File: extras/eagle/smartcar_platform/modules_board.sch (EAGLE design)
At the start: 40 parts

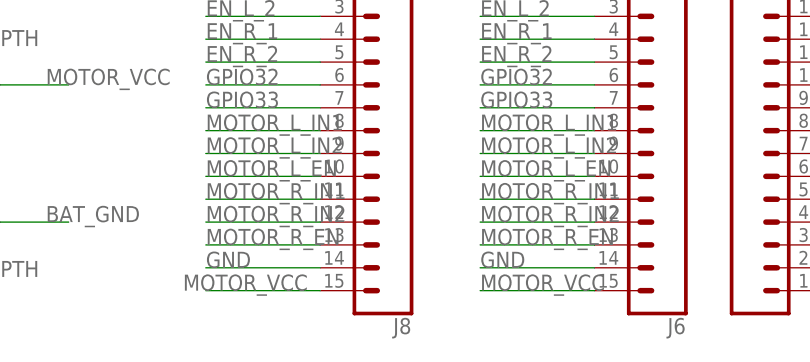
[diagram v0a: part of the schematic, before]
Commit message: Fix ESP32 power supply line to 5V
ESP32 was powered on via its VIN pin which based
on the specs of the ESP32 DOIT devkit is supposed
to handle up to 12V.
This isn't actually the case and anything above 6V
makes the regulator on the board overheat.

Note that the 5V is actually the voltage coming from
our own on-board regulator.
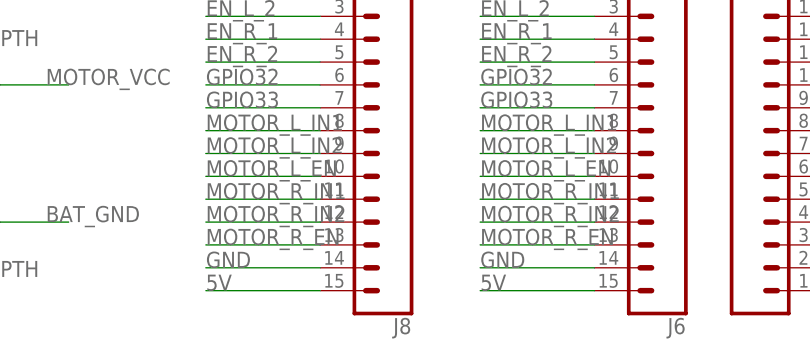
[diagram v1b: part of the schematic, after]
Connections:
- net 5V: now also J6.15, J8.15
- net MOTOR_VCC: no longer J6.15, J8.15
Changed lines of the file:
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@@
 <?xml version="1.0" encoding="utf-8"?>
 <!DOCTYPE eagle SYSTEM "eagle.dtd">
-<eagle version="9.5.2">
+<eagle version="9.6.2">
 <drawing>
 <settings>
@@
 </segment>
 <segment>
-<pinref part="J6" gate="G$1" pin="15"/>
-<wire x1="-73.66" y1="-50.8" x2="-86.36" y2="-50.8" width="0.1524" layer="91"/>
-<label x="-86.36" y="-50.8" size="1.778" layer="95"/>
-</segment>
-<segment>
 <pinref part="5V_REGULATOR" gate="J$1" pin="1"/>
 <wire x1="-134.62" y1="60.96" x2="-127" y2="60.96" width="0.1524" layer="91"/>
 <label x="-129.54" y="60.96" size="1.778" layer="95"/>
-</segment>
-<segment>
-<pinref part="J8" gate="G$1" pin="15"/>
-<wire x1="-104.14" y1="-50.8" x2="-116.84" y2="-50.8" width="0.1524" layer="91"/>
-<label x="-119.38" y="-50.8" size="1.778" layer="95"/>
 </segment>
 <segment>
@@
 <label x="-114.3" y="-7.62" size="1.778" layer="95"/>
 </segment>
-</net>
+<segment>
+<pinref part="J8" gate="G$1" pin="15"/>
+<wire x1="-104.14" y1="-50.8" x2="-116.84" y2="-50.8" width="0.1524" layer="91"/>
+<label x="-116.84" y="-50.8" size="1.778" layer="95"/>
+</segment>
+<segment>
+<pinref part="J6" gate="G$1" pin="15"/>
+<wire x1="-73.66" y1="-50.8" x2="-86.36" y2="-50.8" width="0.1524" layer="91"/>
+<label x="-86.36" y="-50.8" size="1.778" layer="95"/>
+</segment>
+</net>
